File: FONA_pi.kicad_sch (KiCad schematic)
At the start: 19 parts, among them J1 Conn_01x20_Socket, J10 Conn_01x04_Pin, J2 Conn_02x20_Odd_Even, J3 Conn_01x20_Socket, J4 Conn_01x20_Socket, J5 Conn_01x18, J6 Conn_01x18_Socket, J7 Conn_01x20_Socket, J8 Conn_01x18, J9 Conn_01x04_Pin

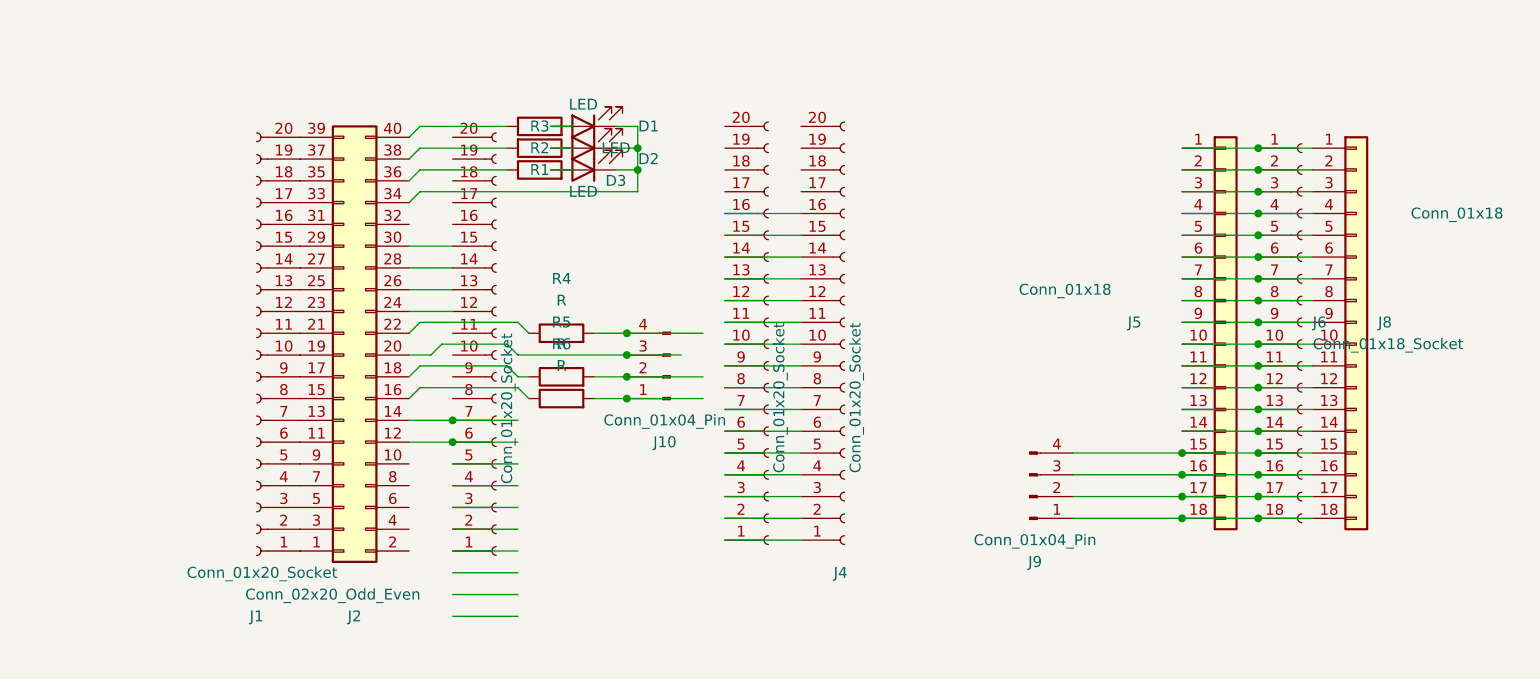
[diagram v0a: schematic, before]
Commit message: lots of pin and trace cleanup
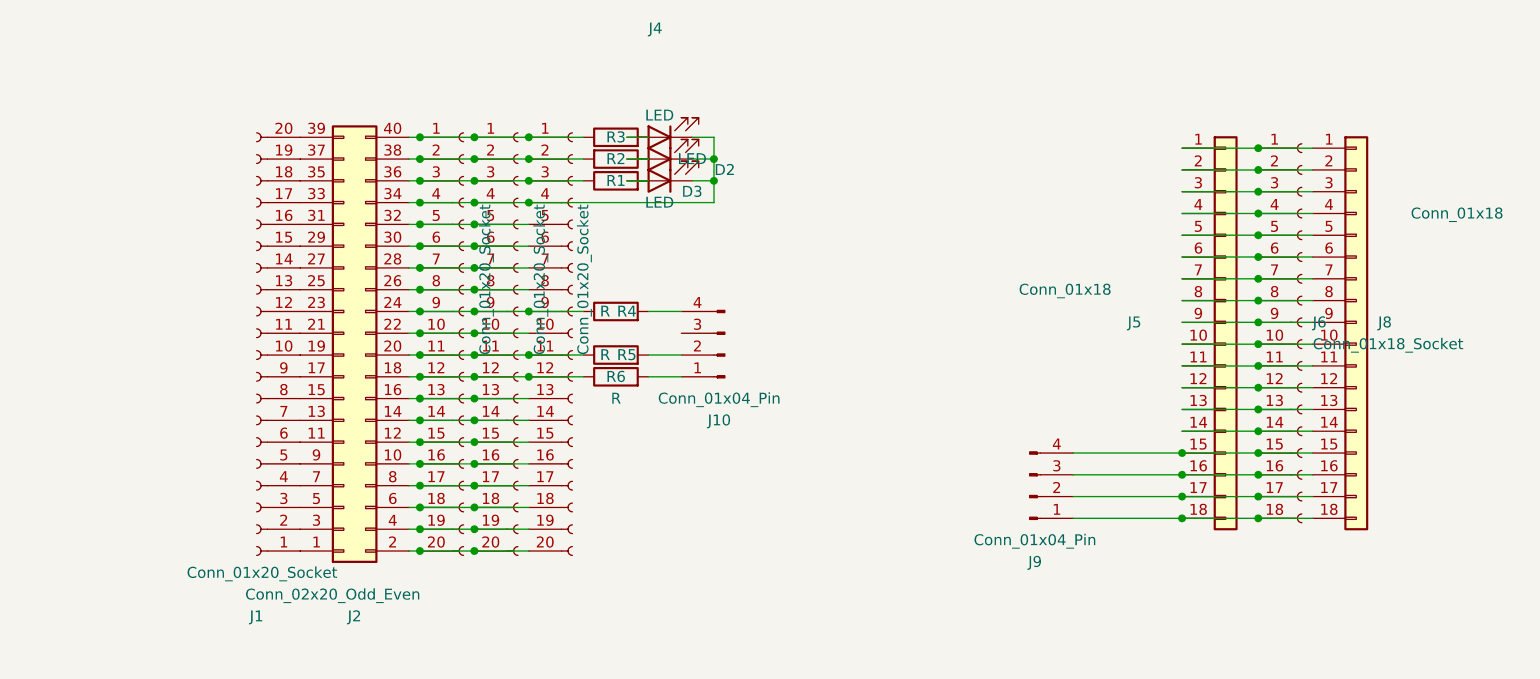
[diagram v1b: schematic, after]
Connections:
- net at J4.1 (Pin_1), J7.1 (Pin_1): now also J2.40 (Pin_40), J3.1 (Pin_1), R3.1
- net at J4.10 (Pin_10), J7.10 (Pin_10): now also J2.22 (Pin_22), J3.10 (Pin_10)
- net at J4.11 (Pin_11), J7.11 (Pin_11): now also J2.20 (Pin_20), J3.11 (Pin_11), R5.1
- net at J4.12 (Pin_12), J7.12 (Pin_12): now also J2.18 (Pin_18), J3.12 (Pin_12), R6.1
- net at J4.13 (Pin_13), J7.13 (Pin_13): now also J2.16 (Pin_16), J3.13 (Pin_13)
- net at J4.14 (Pin_14), J7.14 (Pin_14): now also J2.14 (Pin_14), J3.14 (Pin_14)
- net at J4.15 (Pin_15), J7.15 (Pin_15): now also J2.12 (Pin_12), J3.15 (Pin_15)
- net at J4.16 (Pin_16), J7.16 (Pin_16): now also J2.10 (Pin_10), J3.16 (Pin_16)
- net at J7.17 (Pin_17): now also J2.8 (Pin_8), J3.17 (Pin_17), J4.17 (Pin_17)
- net at J7.18 (Pin_18): now also J2.6 (Pin_6), J3.18 (Pin_18), J4.18 (Pin_18)
- net at J7.19 (Pin_19): now also J2.4 (Pin_4), J3.19 (Pin_19), J4.19 (Pin_19)
- net at J4.2 (Pin_2), J7.2 (Pin_2): now also J2.38 (Pin_38), J3.2 (Pin_2), R2.2
- net at J7.20 (Pin_20): now also J2.2 (Pin_2), J3.20 (Pin_20), J4.20 (Pin_20)
- net at J4.3 (Pin_3), J7.3 (Pin_3): now also J2.36 (Pin_36), J3.3 (Pin_3), R1.1
- net at J4.4 (Pin_4), J7.4 (Pin_4): now also D1.1 (K), D2.1 (K), D3.1 (K), J2.34 (Pin_34), J3.4 (Pin_4)
- net at J4.5 (Pin_5), J7.5 (Pin_5): now also J2.32 (Pin_32), J3.5 (Pin_5)
- net at J4.6 (Pin_6), J7.6 (Pin_6): now also J2.30 (Pin_30), J3.6 (Pin_6)
- net at J4.7 (Pin_7), J7.7 (Pin_7): now also J2.28 (Pin_28), J3.7 (Pin_7)
- net at J4.8 (Pin_8), J7.8 (Pin_8): now also J2.26 (Pin_26), J3.8 (Pin_8)
- net at J4.9 (Pin_9), J7.9 (Pin_9): now also J2.24 (Pin_24), J3.9 (Pin_9), R4.1
- net at J10.3 (Pin_3): no longer J2.20 (Pin_20)
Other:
- moved on the sheet: D2, D3, J10, J4, R1, R2, R3, R4, R5, R6

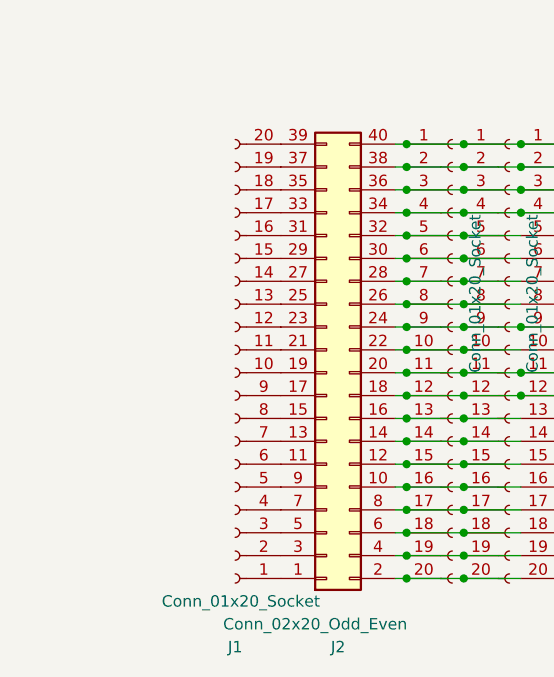
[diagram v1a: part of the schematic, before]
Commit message: Added two more rails for the left side of the Rpi0
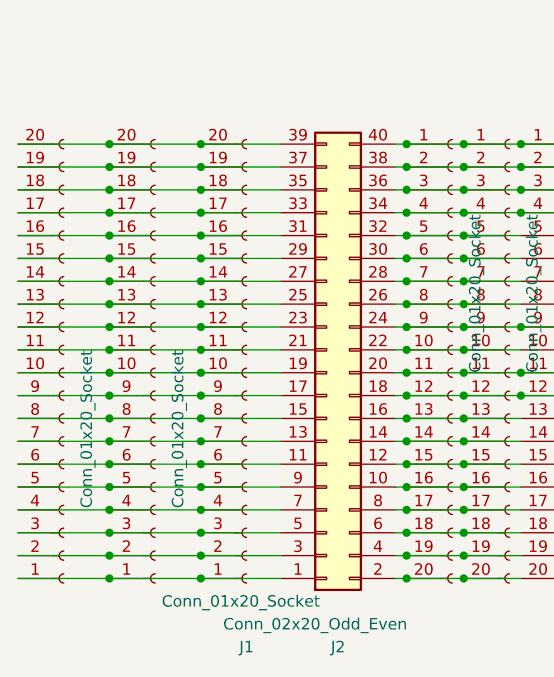
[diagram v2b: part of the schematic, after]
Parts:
- added J11, J12: Conn_01x20_Socket, Connector_PinSocket_2.54mm:PinSocket_1x20_P2.54mm_Vertical, symbol Connector:Conn_01x20_Socket
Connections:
- net at J1.1 (Pin_1), J2.1 (Pin_1): now also J11.1 (Pin_1), J12.1 (Pin_1)
- net at J1.6 (Pin_6), J2.11 (Pin_11): now also J11.6 (Pin_6), J12.6 (Pin_6)
- net at J1.7 (Pin_7), J2.13 (Pin_13): now also J11.7 (Pin_7), J12.7 (Pin_7)
- net at J1.8 (Pin_8), J2.15 (Pin_15): now also J11.8 (Pin_8), J12.8 (Pin_8)
- net at J1.9 (Pin_9), J2.17 (Pin_17): now also J11.9 (Pin_9), J12.9 (Pin_9)
- net at J1.10 (Pin_10), J2.19 (Pin_19): now also J11.10 (Pin_10), J12.10 (Pin_10)
- net at J1.11 (Pin_11), J2.21 (Pin_21): now also J11.11 (Pin_11), J12.11 (Pin_11)
- net at J1.12 (Pin_12), J2.23 (Pin_23): now also J11.12 (Pin_12), J12.12 (Pin_12)
- net at J1.13 (Pin_13), J2.25 (Pin_25): now also J11.13 (Pin_13), J12.13 (Pin_13)
- net at J1.14 (Pin_14), J2.27 (Pin_27): now also J11.14 (Pin_14), J12.14 (Pin_14)
- net at J1.15 (Pin_15), J2.29 (Pin_29): now also J11.15 (Pin_15), J12.15 (Pin_15)
- net at J1.2 (Pin_2), J2.3 (Pin_3): now also J11.2 (Pin_2), J12.2 (Pin_2)
- net at J1.16 (Pin_16), J2.31 (Pin_31): now also J11.16 (Pin_16), J12.16 (Pin_16)
- net at J1.17 (Pin_17), J2.33 (Pin_33): now also J11.17 (Pin_17), J12.17 (Pin_17)
- net at J1.18 (Pin_18), J2.35 (Pin_35): now also J11.18 (Pin_18), J12.18 (Pin_18)
- net at J1.19 (Pin_19), J2.37 (Pin_37): now also J11.19 (Pin_19), J12.19 (Pin_19)
- net at J1.20 (Pin_20), J2.39 (Pin_39): now also J11.20 (Pin_20), J12.20 (Pin_20)
- net at J1.3 (Pin_3), J2.5 (Pin_5): now also J11.3 (Pin_3), J12.3 (Pin_3)
- net at J1.4 (Pin_4), J2.7 (Pin_7): now also J11.4 (Pin_4), J12.4 (Pin_4)
- net at J1.5 (Pin_5), J2.9 (Pin_9): now also J11.5 (Pin_5), J12.5 (Pin_5)
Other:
- moved on the sheet: J1

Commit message: tweaks after running DRC
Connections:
- net at J2.22 (Pin_22), J3.10 (Pin_10), J4.10 (Pin_10)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: now also R4.1
- net at J2.20 (Pin_20), J3.11 (Pin_11), J4.11 (Pin_11)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: no longer R5.1
- net at J2.18 (Pin_18), J3.12 (Pin_12), J4.12 (Pin_12)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: now also R5.1; no longer R6.1
- net at J2.16 (Pin_16), J3.13 (Pin_13), J4.13 (Pin_13)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: now also R6.1
- net at J2.24 (Pin_24), J3.9 (Pin_9), J4.9 (Pin_9)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: no longer R4.1
- net at J1.1 (Pin_1), J11.1 (Pin_1), J12.1 (Pin_1)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: now also J10.3 (Pin_3)
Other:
- moved on the sheet: J10, R4, R5, R6

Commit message: Made a bunch of warning fixes.  Silkscreen lettering, etc
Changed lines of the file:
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@@
       (effects (font (size 1.27 1.27)) (justify left) hide)
     )
-    (property "Value" "Conn_01x20_Socket" (at 52.07 90.17 90)
+    (property "Value" "Conn_01x20_Socket" (at 40.64 60.96 0)
       (effects (font (size 1.27 1.27)) (justify left))
     )
@@
       (effects (font (size 1.27 1.27)) (justify left) hide)
     )
-    (property "Value" "Conn_01x20_Socket" (at 41.91 90.17 90)
+    (property "Value" "Conn_01x20_Socket" (at 30.48 55.88 0)
       (effects (font (size 1.27 1.27)) (justify left))
     )
@@
       (effects (font (size 1.27 1.27)) (justify left) hide)
     )
-    (property "Value" "Conn_01x20_Socket" (at 85.09 92.71 90)
+    (property "Value" "Conn_01x20_Socket" (at 72.39 54.61 0)
       (effects (font (size 1.27 1.27)) (justify left))
     )
@@
   (symbol (lib_id "Connector:Conn_01x20_Socket") (at 95.25 90.17 0) (unit 1)
     (in_bom yes) (on_board yes) (dnp no)
-    (property "Reference" "J4" (at 104.14 54.61 0)
-      (effects (font (size 1.27 1.27)) (justify left))
-    )
-    (property "Value" "Conn_01x20_Socket" (at 96.52 92.71 90)
+    (property "Reference" "J4" (at 93.98 58.42 0)
+      (effects (font (size 1.27 1.27)) (justify left))
+    )
+    (property "Value" "Conn_01x20_Socket" (at 105.41 62.23 0)
       (effects (font (size 1.27 1.27)) (justify right))
     )

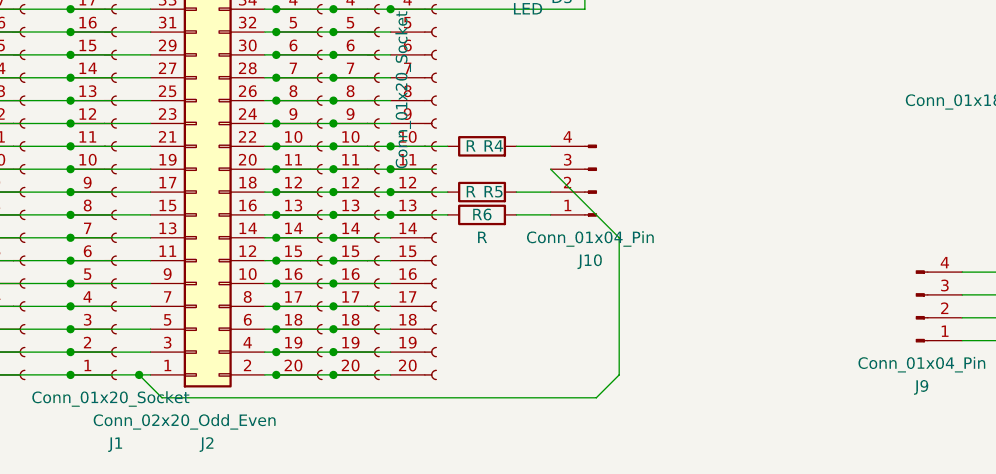
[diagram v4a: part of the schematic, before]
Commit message: Added isolated proto area
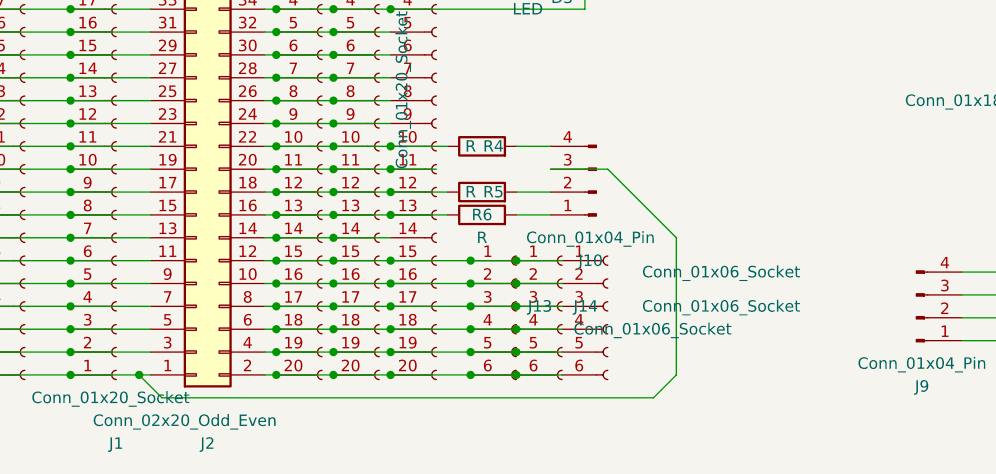
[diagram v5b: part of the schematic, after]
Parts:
- added J13, J14, J15: Conn_01x06_Socket, Connector_PinSocket_2.54mm:PinSocket_1x06_P2.54mm_Vertical, symbol Connector:Conn_01x06_Socket
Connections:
- net at J2.12 (Pin_12), J3.15 (Pin_15), J4.15 (Pin_15)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: now also J13.1 (Pin_1), J14.1 (Pin_1), J15.1 (Pin_1)
- net at J2.10 (Pin_10), J3.16 (Pin_16), J4.16 (Pin_16)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: now also J13.2 (Pin_2), J14.2 (Pin_2), J15.2 (Pin_2)
- net at J2.8 (Pin_8), J3.17 (Pin_17), J4.17 (Pin_17)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: now also J13.3 (Pin_3), J14.3 (Pin_3), J15.3 (Pin_3)
- net at J2.6 (Pin_6), J3.18 (Pin_18), J4.18 (Pin_18)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: now also J13.4 (Pin_4), J14.4 (Pin_4), J15.4 (Pin_4)
- net at J2.4 (Pin_4), J3.19 (Pin_19), J4.19 (Pin_19)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: now also J13.5 (Pin_5), J14.5 (Pin_5), J15.5 (Pin_5)
- net at J2.2 (Pin_2), J3.20 (Pin_20), J4.20 (Pin_20)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: now also J13.6 (Pin_6), J14.6 (Pin_6), J15.6 (Pin_6)

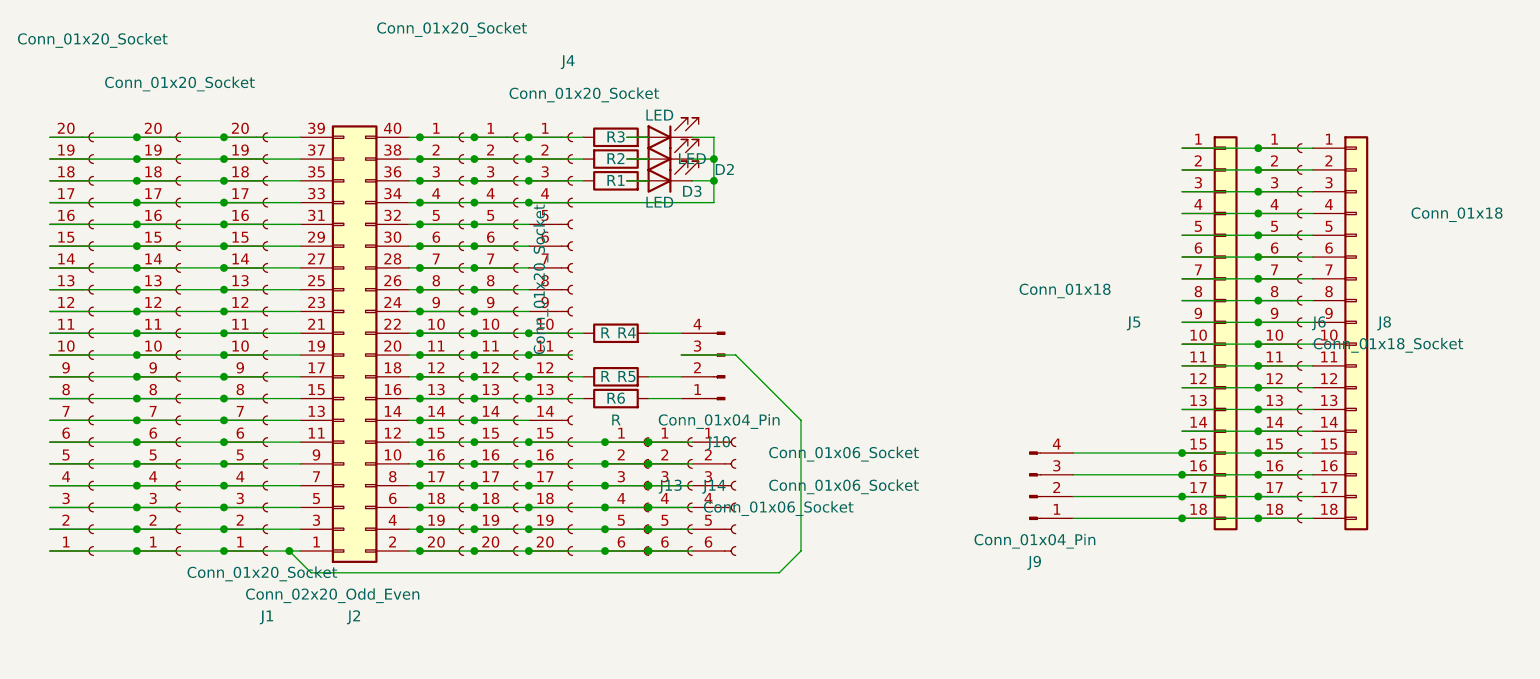
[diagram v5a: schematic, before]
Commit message: Added power and ground rails
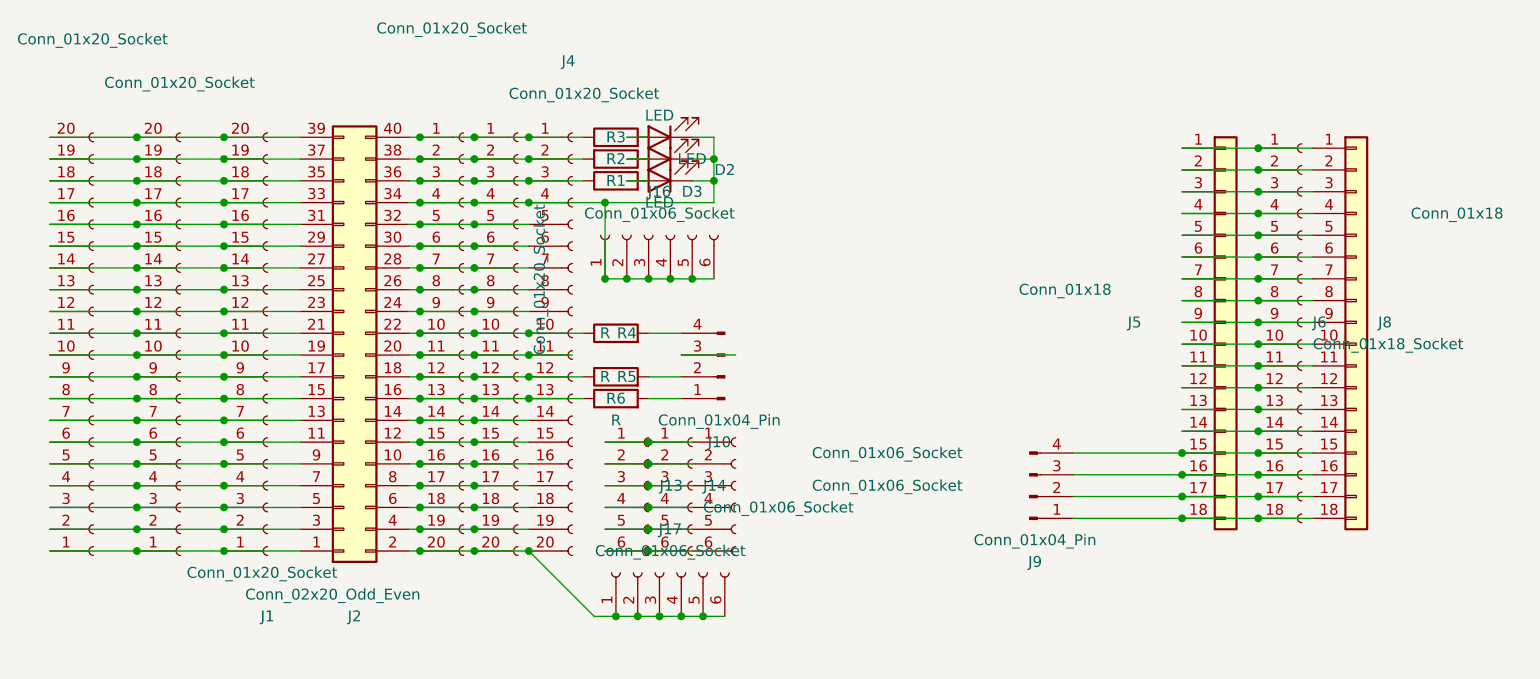
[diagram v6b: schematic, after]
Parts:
- added J16, J17: Conn_01x06_Socket, Connector_PinSocket_2.54mm:PinSocket_1x06_P2.54mm_Vertical, symbol Connector:Conn_01x06_Socket
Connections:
- net at J2.12 (Pin_12), J3.15 (Pin_15), J4.15 (Pin_15)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: no longer J13.1 (Pin_1), J14.1 (Pin_1), J15.1 (Pin_1)
- net at J2.10 (Pin_10), J3.16 (Pin_16), J4.16 (Pin_16)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: no longer J13.2 (Pin_2), J14.2 (Pin_2), J15.2 (Pin_2)
- net at J2.8 (Pin_8), J3.17 (Pin_17), J4.17 (Pin_17)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: no longer J13.3 (Pin_3), J14.3 (Pin_3), J15.3 (Pin_3)
- net at J2.6 (Pin_6), J3.18 (Pin_18), J4.18 (Pin_18)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: no longer J13.4 (Pin_4), J14.4 (Pin_4), J15.4 (Pin_4)
- net at J2.4 (Pin_4), J3.19 (Pin_19), J4.19 (Pin_19)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: no longer J13.5 (Pin_5), J14.5 (Pin_5), J15.5 (Pin_5)
- net at J2.2 (Pin_2), J3.20 (Pin_20), J4.20 (Pin_20)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: now also J17.1 (Pin_1), J17.2 (Pin_2), J17.3 (Pin_3), J17.4 (Pin_4), J17.5 (Pin_5), J17.6 (Pin_6); no longer J13.6 (Pin_6), J14.6 (Pin_6), J15.6 (Pin_6)
- net at D1.1 (K), D2.1 (K), D3.1 (K)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: now also J16.1 (Pin_1), J16.2 (Pin_2), J16.3 (Pin_3), J16.4 (Pin_4), J16.5 (Pin_5), J16.6 (Pin_6)
- net at J1.1 (Pin_1), J11.1 (Pin_1), J12.1 (Pin_1)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: no longer J10.3 (Pin_3)
- new net: J13.1 (Pin_1), J14.1 (Pin_1), J15.1 (Pin_1)
- new net: J13.2 (Pin_2), J14.2 (Pin_2), J15.2 (Pin_2)
- new net: J13.3 (Pin_3), J14.3 (Pin_3), J15.3 (Pin_3)
- new net: J13.4 (Pin_4), J14.4 (Pin_4), J15.4 (Pin_4)
- new net: J13.5 (Pin_5), J14.5 (Pin_5), J15.5 (Pin_5)
- new net: J13.6 (Pin_6), J14.6 (Pin_6), J15.6 (Pin_6)
